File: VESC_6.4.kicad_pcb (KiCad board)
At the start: 4 copper layers, 62 x 60 mm, 428 parts, among them J1 CAN, J10 SUPPLY, J11 GND, J2 HALL_ENC, J3 COMM, J4 SERVO, J5 SWD, J6 USB_OTG, J7 PH_A, J8 PH_B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

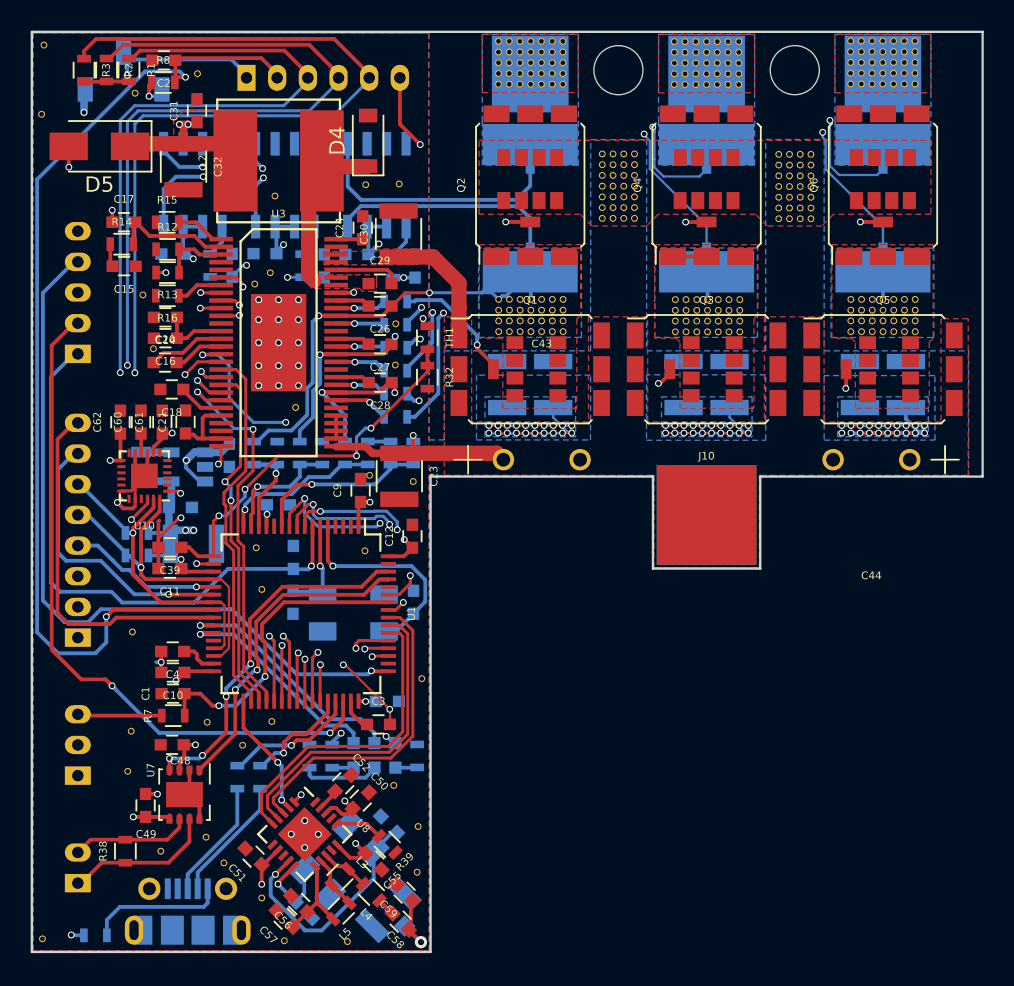
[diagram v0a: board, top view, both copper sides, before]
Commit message: rounded the PCB corners
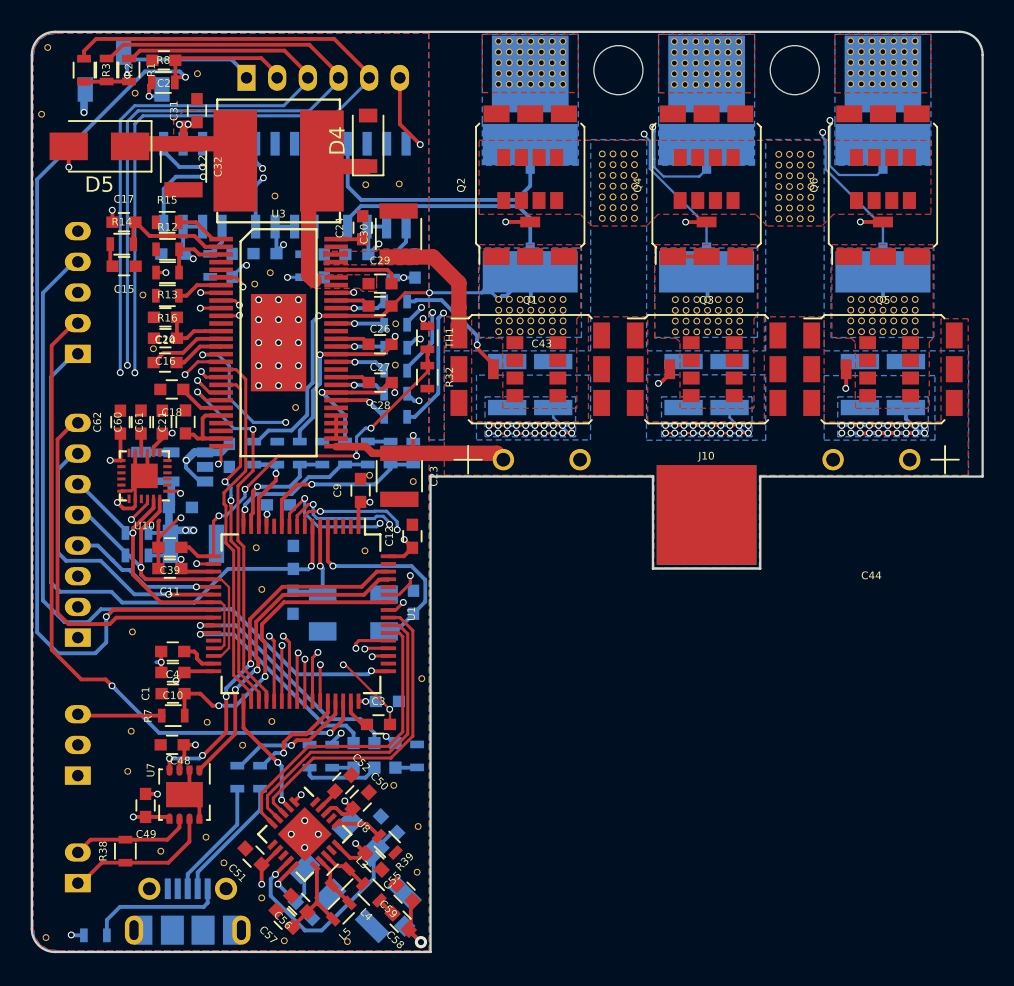
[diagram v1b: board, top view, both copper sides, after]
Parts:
- moved ? 0.29 mm to (123.7, 65.6)
- moved ? 0.25 mm to (123.6, 123.7)
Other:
- outline, holes or cut-outs redrawn
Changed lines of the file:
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@@
   (general
     (thickness 1.6)
-    (drawings 11)
+    (drawings 14)
     (tracks 1571)
     (zones 0)
@@
   )
   (setup
-    (last_trace_width 0.5)
+    (last_trace_width 0.25)
     (user_trace_width 0.15)
     (user_trace_width 0.2)
@@
     (trace_min 0.13)
     (segment_width 0.2)
-    (edge_width 0.15)
+    (edge_width 0.2)
     (via_size 0.8)
     (via_drill 0.4)
@@
   )
   (module Global_Parts:via-0.45mm (layer F.Cu)
-    (at 123.39828 123.7488)
+    (at 123.63196 123.66752)
     (fp_text reference "" (at 0 0.508) (layer F.SilkS) hide
       (effects (font (size 0.127 0.127) (thickness 0.03175)))
@@
   )
   (module Global_Parts:via-0.45mm (layer F.Cu)
-    (at 123.49734 65.47104)
+    (at 123.74372 65.62852)
     (fp_text reference "" (at 0 0.508) (layer F.SilkS) hide
       (effects (font (size 0.127 0.127) (thickness 0.03175)))
@@
     )
   )
+  (gr_arc (start 183.2074 66.1049) (end 184.7074 66.1049) (angle -90.1) (layer Edge.Cuts) (width 0.15))
+  (gr_arc (start 124.2074 123.1049) (end 122.7074 123.1049) (angle -90) (layer Edge.Cuts) (width 0.15))
+  (gr_arc (start 124.2074 66.1049) (end 124.2074 64.6049) (angle -90) (layer Edge.Cuts) (width 0.15))
   (gr_text "Rev1a\n3/4/2018" (at 133.13918 118.3894) (layer B.SilkS)
     (effects (font (size 0.75 0.75) (thickness 0.1875)) (justify mirror))
@@
   (gr_line (start 163.2074 99.6049) (end 170.2074 99.6049) (layer Edge.Cuts) (width 0.15))
   (gr_line (start 163.2074 93.6049) (end 163.2074 99.6049) (layer Edge.Cuts) (width 0.15))
-  (gr_line (start 122.7074 64.6049) (end 184.7074 64.6049) (layer Edge.Cuts) (width 0.15))
-  (gr_line (start 184.7074 64.6049) (end 184.7074 93.6049) (layer Edge.Cuts) (width 0.15))
+  (gr_line (start 124.2074 64.6049) (end 183.2074 64.6049) (layer Edge.Cuts) (width 0.15))
+  (gr_line (start 184.7074 66.1049) (end 184.7074 93.6049) (layer Edge.Cuts) (width 0.15))
   (gr_line (start 148.7074 93.6049) (end 163.2074 93.6049) (layer Edge.Cuts) (width 0.15))
   (gr_line (start 170.2074 93.6049) (end 170.2074 99.6049) (layer Edge.Cuts) (width 0.15))
   (gr_line (start 170.2074 93.6049) (end 184.7074 93.6049) (layer Edge.Cuts) (width 0.15))
   (gr_line (start 148.7074 93.6049) (end 148.7074 124.6049) (layer Edge.Cuts) (width 0.15))
-  (gr_line (start 122.7074 124.6049) (end 148.7074 124.6049) (layer Edge.Cuts) (width 0.15))
-  (gr_line (start 122.7074 64.6049) (end 122.7074 124.6049) (layer Edge.Cuts) (width 0.15))
+  (gr_line (start 124.2074 124.6049) (end 148.7074 124.6049) (layer Edge.Cuts) (width 0.15))
+  (gr_line (start 122.7074 66.1049) (end 122.7074 123.1049) (layer Edge.Cuts) (width 0.15))
   (segment (start 134.48538 108.5469) (end 133.69798 107.7595) (width 0.25) (layer F.Cu) (net 1))
   (segment (start 133.69798 107.7595) (end 132.6649 107.7595) (width 0.25) (layer F.Cu) (net 1))
@@
     (polygon
       (pts
-        (xy 122.7836 64.6811) (xy 122.7836 124.5235) (xy 148.6281 124.5235) (xy 148.59 64.6938)
+        (xy 124.23648 64.67856) (xy 123.70816 64.78524) (xy 123.2408 65.09004) (xy 122.93092 65.51676) (xy 122.7836 66.0908)
+        (xy 122.7836 122.90044) (xy 122.88012 123.5964) (xy 123.22048 124.10948) (xy 123.76404 124.44984) (xy 124.39396 124.5235)
+        (xy 148.6281 124.5235) (xy 148.59 64.6938)
       )
     )
@@
     (polygon
       (pts
-        (xy 122.7836 64.6811) (xy 122.7836 124.52858) (xy 148.6281 124.5235) (xy 148.6027 64.6938)
+        (xy 124.388884 64.68189) (xy 123.71832 64.78016) (xy 123.24588 65.08496) (xy 122.93092 65.51168) (xy 122.7836 66.2432)
+        (xy 122.7836 122.8852) (xy 122.87504 123.59132) (xy 123.23064 124.11964) (xy 123.76912 124.45492) (xy 124.490483 124.528245)
+        (xy 148.6281 124.5235) (xy 148.6027 64.6938)
       )
     )
@@
     (polygon
       (pts
-        (xy 148.59 64.692587) (xy 148.606891 91.216382) (xy 149.606 91.216382) (xy 149.606 85.40496) (xy 159.143571 85.40496)
-        (xy 159.154288 71.632982) (xy 162.801728 71.638062) (xy 162.792506 85.40496) (xy 170.561 85.40496) (xy 170.561 71.628)
-        (xy 174.371 71.628) (xy 174.373086 85.4075) (xy 183.7944 85.4075) (xy 183.7944 91.4146) (xy 183.787208 91.4146)
-        (xy 183.787208 93.537942) (xy 170.157568 93.537942) (xy 170.157568 99.562822) (xy 163.258928 99.562822) (xy 163.274168 93.537942)
-        (xy 148.608369 93.537942) (xy 148.6281 124.522287) (xy 122.7836 124.522287) (xy 122.7836 64.679887)
+        (xy 123.71324 64.79032) (xy 124.383796 64.680674) (xy 148.59 64.692587) (xy 148.606891 91.216382) (xy 149.606 91.216382)
+        (xy 149.606 85.40496) (xy 159.143571 85.40496) (xy 159.154288 71.632982) (xy 162.801728 71.638062) (xy 162.792506 85.40496)
+        (xy 170.561 85.40496) (xy 170.561 71.628) (xy 174.371 71.628) (xy 174.373086 85.4075) (xy 183.7944 85.4075)
+        (xy 183.7944 91.4146) (xy 183.787208 91.4146) (xy 183.787208 93.537942) (xy 170.157568 93.537942) (xy 170.157568 99.562822)
+        (xy 163.258928 99.562822) (xy 163.274168 93.537942) (xy 148.608369 93.537942) (xy 148.6281 124.522287) (xy 124.43968 124.522287)
+        (xy 123.78436 124.46) (xy 123.23064 124.11964) (xy 122.88012 123.58624) (xy 122.7836 122.88012) (xy 122.7836 66.23304)
+        (xy 122.93092 65.52692) (xy 123.24588 65.08496)
       )
     )
@@
     (polygon
       (pts
-        (xy 122.7836 64.6811) (xy 122.7836 124.52858) (xy 148.6281 124.5235) (xy 148.6027 64.6938)
+        (xy 124.404119 64.681898) (xy 123.70816 64.78524) (xy 123.23572 65.09004) (xy 122.92584 65.52184) (xy 122.7836 66.21272)
+        (xy 122.7836 122.98172) (xy 122.89536 123.64212) (xy 123.24588 124.13488) (xy 123.75388 124.44984) (xy 124.515884 124.52824)
+        (xy 148.6281 124.5235) (xy 148.6027 64.6938)
       )
     )

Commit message: fixed vias, updated PCB per schematic
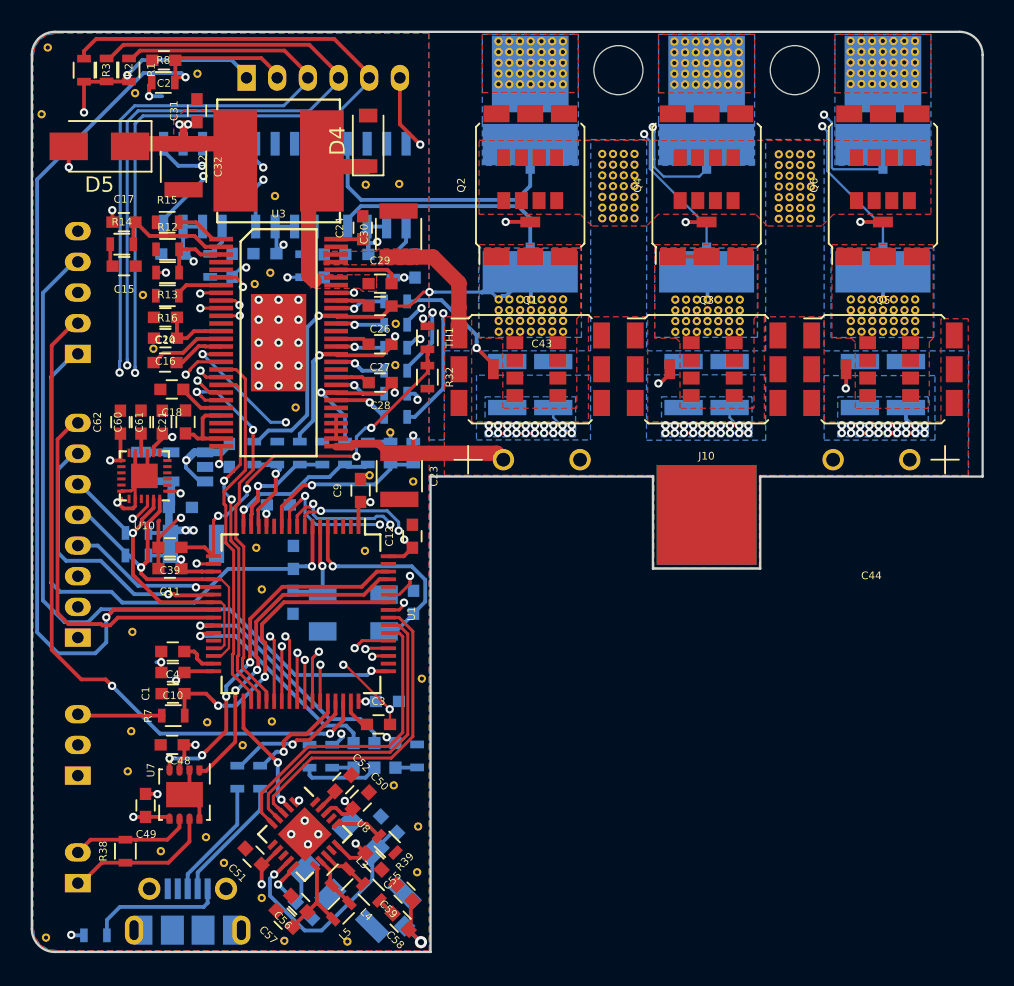
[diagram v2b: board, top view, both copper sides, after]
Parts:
- removed SW1: SENSOR_VOLTAGE, Global_Parts:JS102011JCQN
- added ?: , Kinetic_Footprints:via-0.45mm, F.Cu at (146.1, 90.7)
- ? (x281): footprint Global_Parts:via-0.45mm -> Kinetic_Footprints:via-0.45mm
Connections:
- J2 pad 1: Net-(J2-Pad1) -> +5V
- R1 pad 2: Net-(J2-Pad1) -> +5V
- R2 pad 2: Net-(J2-Pad1) -> +5V
- R3 pad 2: Net-(J2-Pad1) -> +5V
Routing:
- net +5V: track 119.1 -> 132.4 mm, vias 7 -> 8
- net Net-(J2-Pad1): track 13.1 -> 0.00 mm, vias 1 -> 0
- net /DRV/EN_GATE: track 25.8 -> 24.7 mm
- net GND: track 53.4 -> 54.4 mm
- net Net-(R35-Pad2): track 57.0 -> 56.2 mm
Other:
- net class Default: clearance 0.13 -> 0.127
- rule trace_clearance: 0.13 -> 0.127
- rule via_min_drill: 0.3 -> 0.26

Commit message: silkscreen fixes on PCB
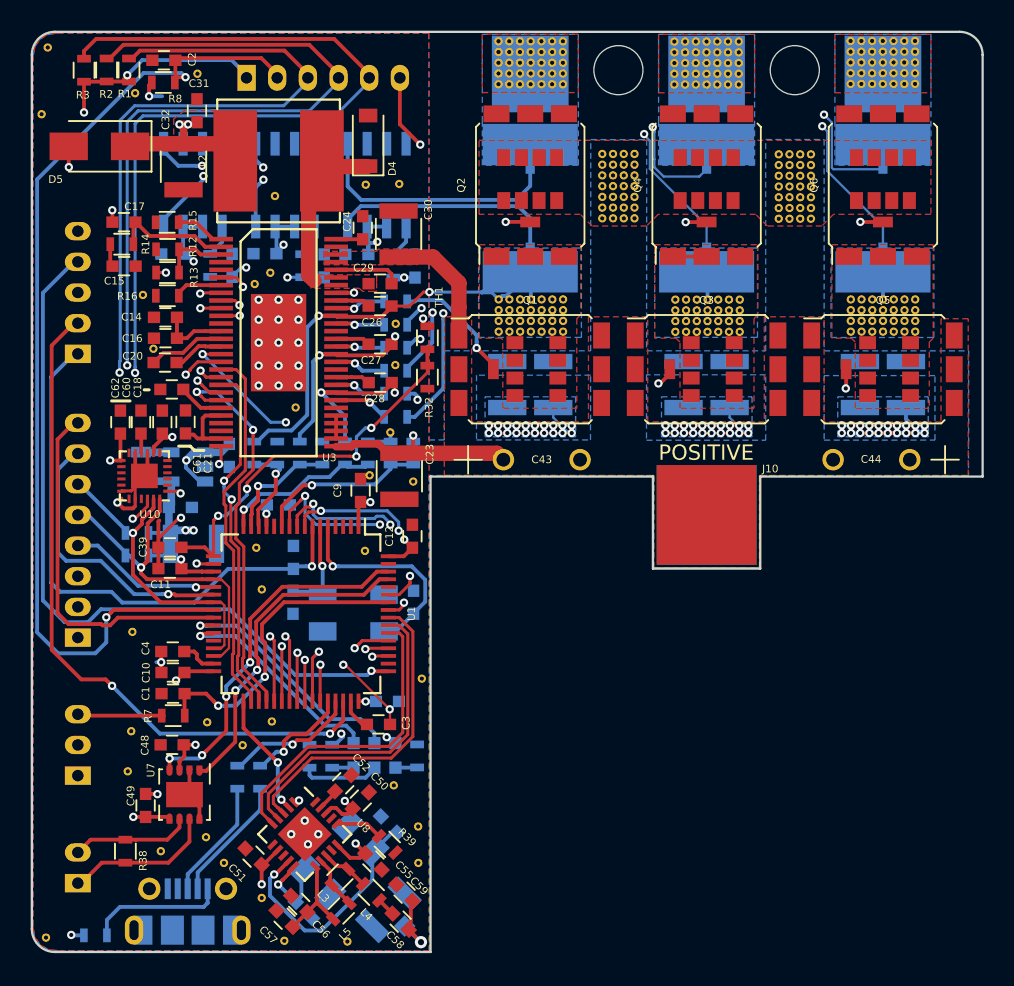
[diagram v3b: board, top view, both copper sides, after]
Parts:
- added G***: OSHW-logo_silkscreen-back_6mm, OSHW_logo:OSHW-logo_silkscreen-back_3mm, B.Cu at (126.3, 68.3)
- moved G*** 38.9 mm to (126.2, 68.4)
- moved ? 0.61 mm to (147.9, 118.8)
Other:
- net class Default: clearance 0.127 -> 0
- rule trace_clearance: 0.127 -> 0
- board text added: "ADC3 MISO ADC2 SCL MOSI TX SDA NSS RX SCK ADC1 GND VCC 5V"
- board text added: "CAN - CAN +"
- board text added: "NEGATIVE"
- board text added: "POSITIVE"
- board text added: "Rev1b 4/14/2018"
- board text added: "SIG 5V GND"
- board text added: "VCC CLK GND IO RST"
- board text removed: "Rev1a 3/4/2018"
